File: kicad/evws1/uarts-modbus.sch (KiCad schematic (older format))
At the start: 40 parts, among them J11 USB 2.0 Mini, J12 USB 2.0 Mini, J15 Jumper, J16 header, J17 header, J18 header, J19 header, J20 header, U10 max485esa, U5 ch340g, U6 ch340g, Y2 12MHz, Y3 12MHz

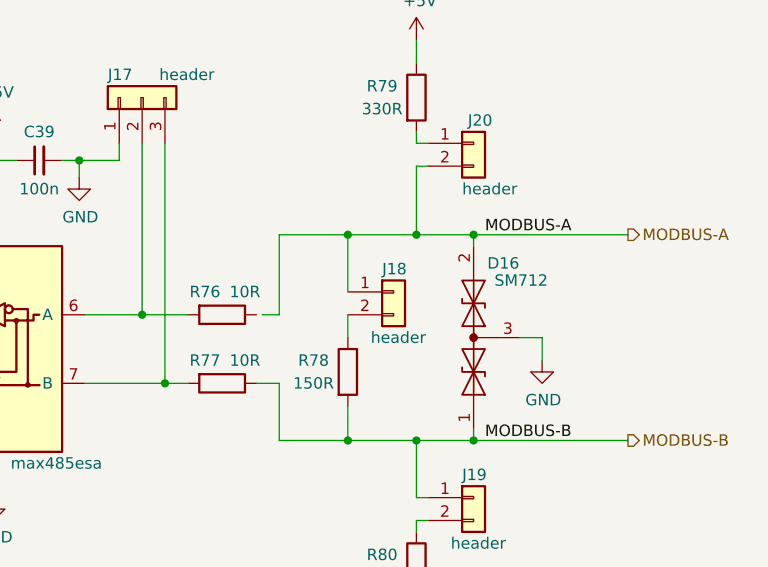
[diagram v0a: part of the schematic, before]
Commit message: Schematic completed, no DRC errors left
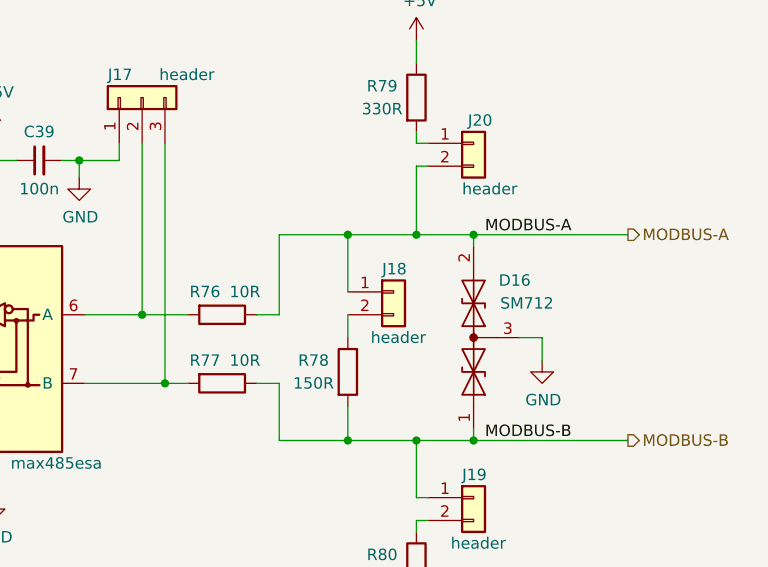
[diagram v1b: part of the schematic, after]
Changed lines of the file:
@@
 U 1 1 5E31D390
 P 9700 4100
-F 0 "D16" V 10025 3900 50  0000 L CNN
-F 1 "SM712" V 9950 3775 50  0000 L CNN
+F 0 "D16" V 9950 3850 50  0000 L CNN
+F 1 "SM712" V 9850 3750 50  0000 L CNN
 F 2 "Project:sot-23_hand-soldering" H 9550 4100 50  0001 C CNN
 F 3 "" H 9550 4100 50  0001 C CNN
@@
 Wire Wire Line
 	9150 4100 9150 4000
-Wire Wire Line
-	8775 4000 8850 4000
 Wire Wire Line
 	8850 4000 8850 3650
@@
 Wire Wire Line
 	9450 2900 9450 2800
+Wire Wire Line
+	8750 4000 8850 4000
 $EndSCHEMATC

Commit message: ...
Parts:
- added TP8, TP9: TestPoint, Wire_Pads:SolderWirePad_single_0-8mmDrill, symbol Connector:TestPoint
- R63, R73, R74, R75, R76, R77, R78, R79, R80: footprint Project:r-0805-hand-soldering -> Project:r-1206-hand-soldering
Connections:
- net labels added: UART0-5V, UART1-5V, USB0-D+, USB0-D-, USB1-D+, USB1-D-
- wire segments 155 -> 159
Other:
- moved on the sheet: C37, C38, D14, D15, F1, F2

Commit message: ...
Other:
- moved on the sheet: J18
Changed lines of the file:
@@
 L Connector_Generic:Conn_01x02 J18
 U 1 1 5E32530C
-P 9350 3900
-F 0 "J18" H 9300 4000 50  0000 L CNN
-F 1 "header" H 9250 3700 50  0000 L CNN
-F 2 "Project:idc-header-1x02-p2.54mm-vertical" H 9350 3900 50  0001 C CNN
-F 3 "~" H 9350 3900 50  0001 C CNN
-	1    9350 3900
-	1    0    0    -1
+P 9350 3950
+F 0 "J18" H 9300 3750 50  0000 L CNN
+F 1 "header" H 9300 4050 50  0000 L CNN
+F 2 "Project:idc-header-1x02-p2.54mm-vertical" H 9350 3950 50  0001 C CNN
+F 3 "~" H 9350 3950 50  0001 C CNN
+	1    9350 3950
+	1    0    0    1
 $EndComp
 $Comp
@@
 $EndComp
 Wire Wire Line
-	9150 4100 9150 4000
+	9150 4100 9150 3950
 Wire Wire Line
 	8850 4000 8850 3650
-Wire Wire Line
-	9150 3900 9150 3650
 Wire Wire Line
 	9700 3700 9700 3650
@@
 Wire Wire Line
 	8350 4000 8450 4000
+Wire Wire Line
+	9150 3850 9150 3650
 $EndSCHEMATC

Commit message: ...
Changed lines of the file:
@@
 	8200 1900 8200 2000
 Wire Wire Line
-	8300 1800 7800 1800
+	8300 1400 7800 1400
 Wire Wire Line
-	8300 1700 7800 1700
+	8300 1300 7800 1300
 Wire Wire Line
 	8300 1600 7800 1600
@@
 	8300 1500 7800 1500
 Wire Wire Line
-	8300 1400 7800 1400
+	8300 1800 7800 1800
 Wire Wire Line
-	8300 1300 7800 1300
+	8300 1700 7800 1700
 Text Label 6600 4100 0    50   ~ 0
 ~RE1
 Text Label 6600 4200 0    50   ~ 0
 DE1
+Text Label 7900 1400 0    50   ~ 0
+DE1
+Text Label 7900 1300 0    50   ~ 0
+~RE1
 Text Label 7900 1800 0    50   ~ 0
-DE1
+UC-TXD0
 Text Label 7900 1700 0    50   ~ 0
-~RE1
-Text Label 7900 1400 0    50   ~ 0
-UC-TXD0
-Text Label 7900 1300 0    50   ~ 0
 UC-RXD0
 Text Label 7900 1500 0    50   ~ 0

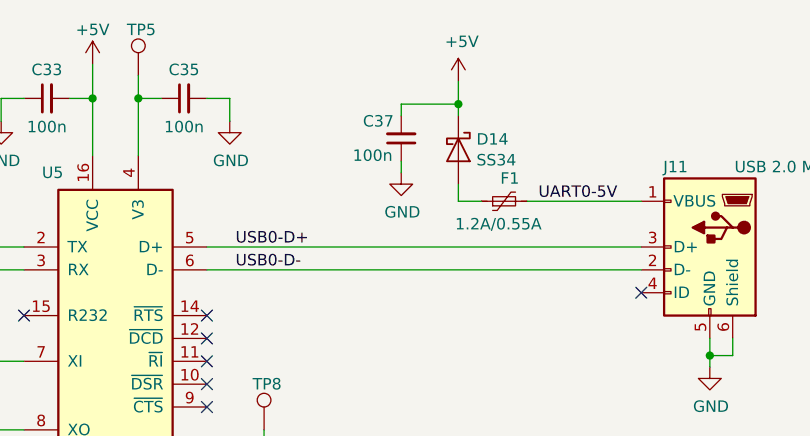
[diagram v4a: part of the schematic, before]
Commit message: first routing finished, clean DRC
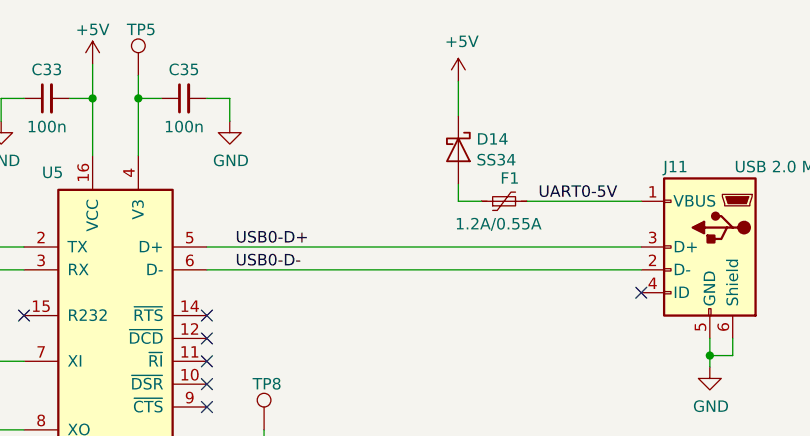
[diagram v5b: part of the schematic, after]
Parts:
- removed C37: 100n, Project:c-1206-hand-soldering, symbol Device:C_Small
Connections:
- wire segments 159 -> 155
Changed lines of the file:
@@
-$EndComp
-$Comp
-L Device:C_Small C?
-U 1 1 5E2A2D0C
-P 4250 1425
-AR Path="/5E0A3961/5E2A2D0C" Ref="C?"  Part="1"
-AR Path="/5E0A3961/5E20BE9A/5E2A2D0C" Ref="C37"  Part="1"
-F 0 "C37" H 4350 1350 50  0000 C CNN
-F 1 "100n" H 4375 1500 50  0000 C CNN
-F 2 "Project:c-1206-hand-soldering" H 4250 1425 50  0001 C CNN
-F 3 "~" H 4250 1425 50  0001 C CNN
-	1    4250 1425
-	-1   0    0    1
-$EndComp
-Wire Wire Line
-	4500 1325 4500 1275
-Wire Wire Line
-	4500 1275 4250 1275
-Wire Wire Line
-	4250 1275 4250 1325
-Connection ~ 4500 1275
-Wire Wire Line
-	4500 1275 4500 1175
-$Comp
-L power:GND #PWR0211
-U 1 1 5E2A2EB7
-P 4250 1575
-F 0 "#PWR0211" H 4250 1325 50  0001 C CNN
-F 1 "GND" H 4255 1402 50  0000 C CNN
-F 2 "" H 4250 1575 50  0001 C CNN
-F 3 "" H 4250 1575 50  0001 C CNN
-	1    4250 1575
-	1    0    0    -1
 $EndComp
 $Comp
@@
 Wire Wire Line
 	5600 2375 5600 2425
-Wire Wire Line
-	4250 1525 4250 1575
 Wire Wire Line
 	4600 1700 4500 1700
@@
 Wire Wire Line
 	9150 3850 9150 3650
+Wire Wire Line
+	4500 1175 4500 1325
 $EndSCHEMATC

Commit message: ...
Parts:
- renumbered C30 to C4, C35 to C5, J15 to JP5, J18 to JP6, J19 to JP7, J20 to JP8, J16 to T1, J17 to T3
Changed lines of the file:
@@
 P 3300 1250
 AR Path="/5E0A3961/5E2A54FC" Ref="C?"  Part="1"
-AR Path="/5E0A3961/5E20BE9A/5E2A54FC" Ref="C35"  Part="1"
-F 0 "C35" V 3425 1250 50  0000 C CNN
+AR Path="/5E0A3961/5E20BE9A/5E2A54FC" Ref="C5"  Part="1"
+F 0 "C5" V 3425 1250 50  0000 C CNN
 F 1 "100n" V 3175 1250 50  0000 C CNN
 F 2 "Project:c-1206-hand-soldering" H 3300 1250 50  0001 C CNN
@@
 P 2200 6675
 AR Path="/5E0A3961/5E2AEE23" Ref="C?"  Part="1"
-AR Path="/5E0A3961/5E20BE9A/5E2AEE23" Ref="C30"  Part="1"
-F 0 "C30" H 2300 6600 50  0000 C CNN
+AR Path="/5E0A3961/5E20BE9A/5E2AEE23" Ref="C4"  Part="1"
+F 0 "C4" H 2300 6600 50  0000 C CNN
 F 1 "22p" H 2325 6750 50  0000 C CNN
 F 2 "Project:c-1206-hand-soldering" H 2200 6675 50  0001 C CNN
@@
 	2500 5825 2850 5825
 $Comp
-L Connector_Generic:Conn_01x03 J15
+L Connector_Generic:Conn_01x03 JP5
 U 1 1 5E2CA290
 P 1825 5400
-F 0 "J15" H 1905 5442 50  0000 L CNN
+F 0 "JP5" H 1905 5442 50  0000 L CNN
 F 1 "Jumper" H 1905 5351 50  0000 L CNN
 F 2 "Project:idc-header-1x03-p2.54mm-vertical" H 1825 5400 50  0001 C CNN
@@
 UC-TXD1
 $Comp
-L Connector_Generic:Conn_01x03 J17
+L Connector_Generic:Conn_01x03 T3
 U 1 1 5E324F71
 P 8250 3050
-F 0 "J17" V 8350 3200 50  0000 R CNN
+F 0 "T3" V 8350 3200 50  0000 R CNN
 F 1 "header" V 8350 2975 50  0000 R CNN
 F 2 "Project:idc-header-1x03-p2.54mm-vertical" H 8250 3050 50  0001 C CNN
@@
 $EndComp
 $Comp
-L Connector_Generic:Conn_01x02 J20
+L Connector_Generic:Conn_01x02 JP8
 U 1 1 5E3251CE
 P 9700 3250
-F 0 "J20" H 9675 3350 50  0000 L CNN
+F 0 "JP8" H 9675 3350 50  0000 L CNN
 F 1 "header" H 9650 3050 50  0000 L CNN
 F 2 "Project:idc-header-1x02-p2.54mm-vertical" H 9700 3250 50  0001 C CNN
@@
 $EndComp
 $Comp
-L Connector_Generic:Conn_01x02 J19
+L Connector_Generic:Conn_01x02 JP7
 U 1 1 5E32525A
 P 9700 4800
-F 0 "J19" H 9650 4900 50  0000 L CNN
+F 0 "JP7" H 9650 4900 50  0000 L CNN
 F 1 "header" H 9600 4600 50  0000 L CNN
 F 2 "Project:idc-header-1x02-p2.54mm-vertical" H 9700 4800 50  0001 C CNN
@@
 $EndComp
 $Comp
-L Connector_Generic:Conn_01x02 J18
+L Connector_Generic:Conn_01x02 JP6
 U 1 1 5E32530C
 P 9350 3950
-F 0 "J18" H 9300 3750 50  0000 L CNN
+F 0 "JP6" H 9300 3750 50  0000 L CNN
 F 1 "header" H 9300 4050 50  0000 L CNN
 F 2 "Project:idc-header-1x02-p2.54mm-vertical" H 9350 3950 50  0001 C CNN
@@
 $EndComp
 $Comp
-L Connector_Generic:Conn_01x07 J16
+L Connector_Generic:Conn_01x07 T1
 U 1 1 5E32575F
 P 8500 1600
-F 0 "J16" H 8500 1200 50  0000 C CNN
+F 0 "T1" H 8500 1200 50  0000 C CNN
 F 1 "header" H 8525 2025 50  0000 C CNN
 F 2 "Project:idc-header-1x07-p2.54mm-vertical" H 8500 1600 50  0001 C CNN

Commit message: V1.0 Design finished
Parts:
- renumbered TP8 to T10, TP9 to T11, TP5 to T8, TP6 to T9
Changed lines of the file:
@@
 encoding utf-8
 Sheet 4 5
-Title ""
-Date ""
-Rev ""
-Comp ""
-Comment1 ""
+Title "Electro Vehicle Wallbox Station 1"
+Date "2020-02-23"
+Rev "V1.0"
+Comp "(C) Manfred Steiner"
+Comment1 "https://github.com/greenenergyprojects/electro-vehicle-wallbox-station/evws1"
 Comment2 ""
 Comment3 ""
@@
 P 3100 1150
 AR Path="/5E0A3961/5E2A603E" Ref="TP?"  Part="1"
-AR Path="/5E0A3961/5E20BE9A/5E2A603E" Ref="TP5"  Part="1"
-F 0 "TP5" H 3050 1350 50  0000 L CNN
+AR Path="/5E0A3961/5E20BE9A/5E2A603E" Ref="T8"  Part="1"
+F 0 "T8" H 3050 1350 50  0000 L CNN
 F 1 "TestPoint" H 3158 1179 50  0001 L CNN
 F 2 "Wire_Pads:SolderWirePad_single_0-8mmDrill" H 3300 1150 50  0001 C CNN
@@
 P 3350 4975
 AR Path="/5E0A3961/5E2AEE03" Ref="TP?"  Part="1"
-AR Path="/5E0A3961/5E20BE9A/5E2AEE03" Ref="TP6"  Part="1"
-F 0 "TP6" H 3300 5175 50  0000 L CNN
+AR Path="/5E0A3961/5E20BE9A/5E2AEE03" Ref="T9"  Part="1"
+F 0 "T9" H 3300 5175 50  0000 L CNN
 F 1 "TestPoint" H 3408 5004 50  0001 L CNN
 F 2 "Wire_Pads:SolderWirePad_single_0-8mmDrill" H 3550 4975 50  0001 C CNN
@@
 	8200 1900 8200 2000
 Wire Wire Line
+	8300 1500 7800 1500
+Wire Wire Line
+	8300 1600 7800 1600
+Wire Wire Line
 	8300 1400 7800 1400
 Wire Wire Line
 	8300 1300 7800 1300
-Wire Wire Line
-	8300 1600 7800 1600
-Wire Wire Line
-	8300 1500 7800 1500
 Wire Wire Line
 	8300 1800 7800 1800
@@
 Text Label 6600 4200 0    50   ~ 0
 DE1
-Text Label 7900 1400 0    50   ~ 0
+Text Label 7900 1500 0    50   ~ 0
 DE1
-Text Label 7900 1300 0    50   ~ 0
+Text Label 7900 1600 0    50   ~ 0
 ~RE1
 Text Label 7900 1800 0    50   ~ 0
@@
 Text Label 7900 1700 0    50   ~ 0
 UC-RXD0
-Text Label 7900 1500 0    50   ~ 0
+Text Label 7900 1300 0    50   ~ 0
 UC-RXD1
-Text Label 7900 1600 0    50   ~ 0
+Text Label 7900 1400 0    50   ~ 0
 UC-TXD1
 $Comp
@@
 P 3650 2700
 AR Path="/5E0A3961/601D002C" Ref="TP?"  Part="1"
-AR Path="/5E0A3961/5E20BE9A/601D002C" Ref="TP8"  Part="1"
-F 0 "TP8" H 3600 2900 50  0000 L CNN
+AR Path="/5E0A3961/5E20BE9A/601D002C" Ref="T10"  Part="1"
+F 0 "T10" H 3600 2900 50  0000 L CNN
 F 1 "TestPoint" H 3708 2729 50  0001 L CNN
 F 2 "Wire_Pads:SolderWirePad_single_0-8mmDrill" H 3850 2700 50  0001 C CNN
@@
 P 3900 6550
 AR Path="/5E0A3961/601D0033" Ref="TP?"  Part="1"
-AR Path="/5E0A3961/5E20BE9A/601D0033" Ref="TP9"  Part="1"
-F 0 "TP9" H 3850 6750 50  0000 L CNN
+AR Path="/5E0A3961/5E20BE9A/601D0033" Ref="T11"  Part="1"
+F 0 "T11" H 3850 6750 50  0000 L CNN
 F 1 "TestPoint" H 3958 6579 50  0001 L CNN
 F 2 "Wire_Pads:SolderWirePad_single_0-8mmDrill" H 4100 6550 50  0001 C CNN
